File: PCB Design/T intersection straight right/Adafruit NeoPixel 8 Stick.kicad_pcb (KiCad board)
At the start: 2 copper layers, 36.6 x 28.6 mm, 8 parts, among them CN1 1X4SMT, CN2 1X4SMT, CN3 1X4SMT

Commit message: t straight fix
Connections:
- CN3 pad 3: Net-(CN3-Pad3) -> GND
- D4 pad 2: Net-(CN3-Pad3) -> unconnected-(D4-Pad2)
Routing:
- net Net-(CN3-Pad3): track 3.24 -> 0.00 mm, vias 1 -> 0
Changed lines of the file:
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@@
   (net 5 "+5V")
   (net 6 "Net-(CN2-Pad3)")
-  (net 7 "Net-(CN3-Pad3)")
+  (net 7 "unconnected-(D4-Pad2)")
   (net 8 "Net-(CN3-Pad4)")
   (net 9 "Net-(D1-Pad2)")
@@
       (net 5 "+5V") (pinfunction "VDD") (pintype "power_in"))
     (pad "2" smd rect (at -2.45 1.6 90) (size 1.5 1) (layers "F.Cu" "F.Paste" "F.Mask")
-      (net 7 "Net-(CN3-Pad3)") (pinfunction "DOUT") (pintype "output"))
+      (net 7 "unconnected-(D4-Pad2)") (pinfunction "DOUT") (pintype "output"))
     (pad "3" smd rect (at 2.45 1.6 90) (size 1.5 1) (layers "F.Cu" "F.Paste" "F.Mask")
       (net 1 "GND") (pinfunction "VSS") (pintype "power_in"))
@@
       (net 3 "Net-(CN1-Pad2)") (pinfunction "2") (pintype "bidirectional") (solder_mask_margin 0.1016))
     (pad "3" smd rect (at -0.92 0 180) (size 1.5 3.8) (layers "B.Cu" "B.Paste" "B.Mask")
-      (net 7 "Net-(CN3-Pad3)") (pinfunction "3") (pintype "bidirectional") (solder_mask_margin 0.1016))
+      (net 1 "GND") (pinfunction "3") (pintype "bidirectional") (solder_mask_margin 0.1016))
     (pad "4" smd rect (at 2.08 0 180) (size 1.5 3.8) (layers "B.Cu" "B.Paste" "B.Mask")
       (net 8 "Net-(CN3-Pad4)") (pinfunction "4") (pintype "bidirectional") (solder_mask_margin 0.1016))
@@
   (via (at 125.984 102.87) (size 0.8) (drill 0.4) (layers "F.Cu" "B.Cu") (net 5))
   (via (at 155.702 106.172) (size 0.8) (drill 0.4) (layers "F.Cu" "B.Cu") (net 6))
-  (segment (start 142.316 94.564) (end 142.316 97.7) (width 0.25) (layer "F.Cu") (net 7))
-  (segment (start 142.24 94.488) (end 142.316 94.564) (width 0.25) (layer "F.Cu") (net 7))
-  (via (at 142.24 94.488) (size 0.8) (drill 0.4) (layers "F.Cu" "B.Cu") (net 7))
   (via (at 139.192 92.964) (size 0.8) (drill 0.4) (layers "F.Cu" "B.Cu") (net 8))
   (segment (start 148.151782 104.233041) (end 148.151782 106.481782) (width 0.25) (layer "F.Cu") (net 9))

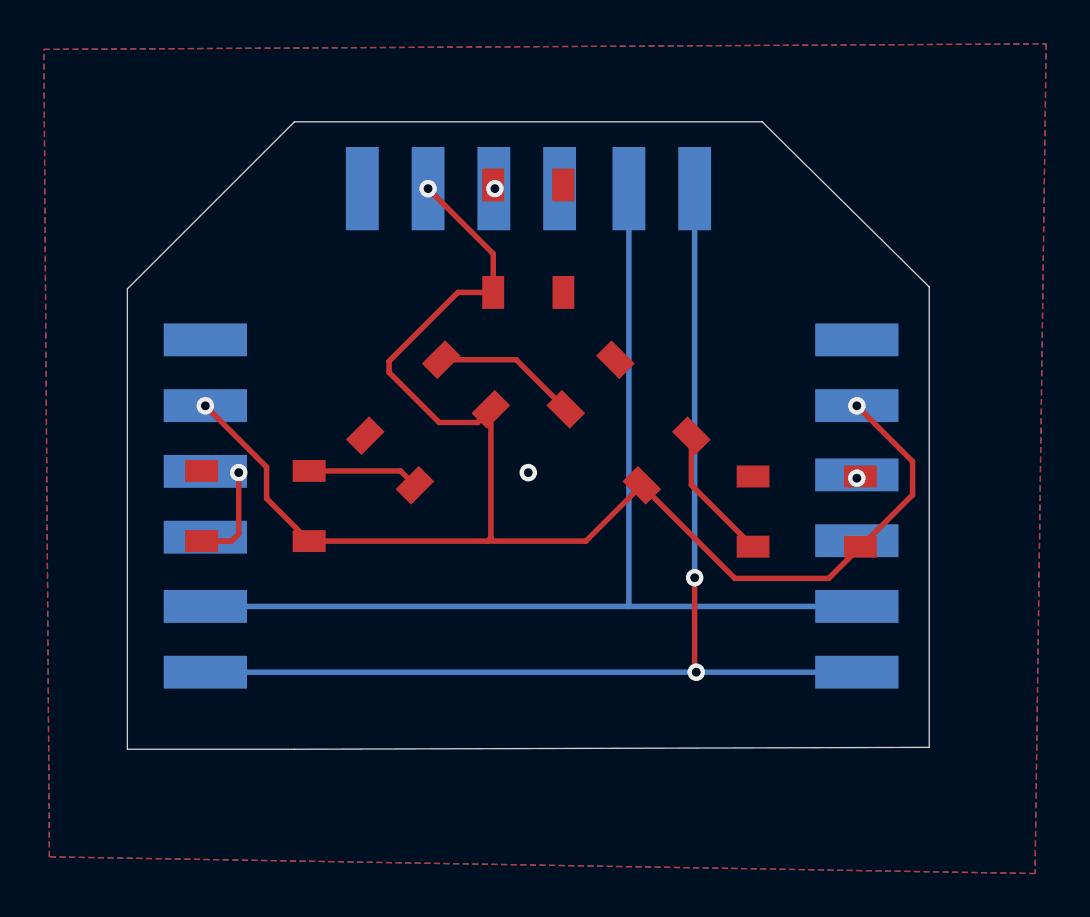
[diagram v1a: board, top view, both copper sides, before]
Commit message: move vias off pads
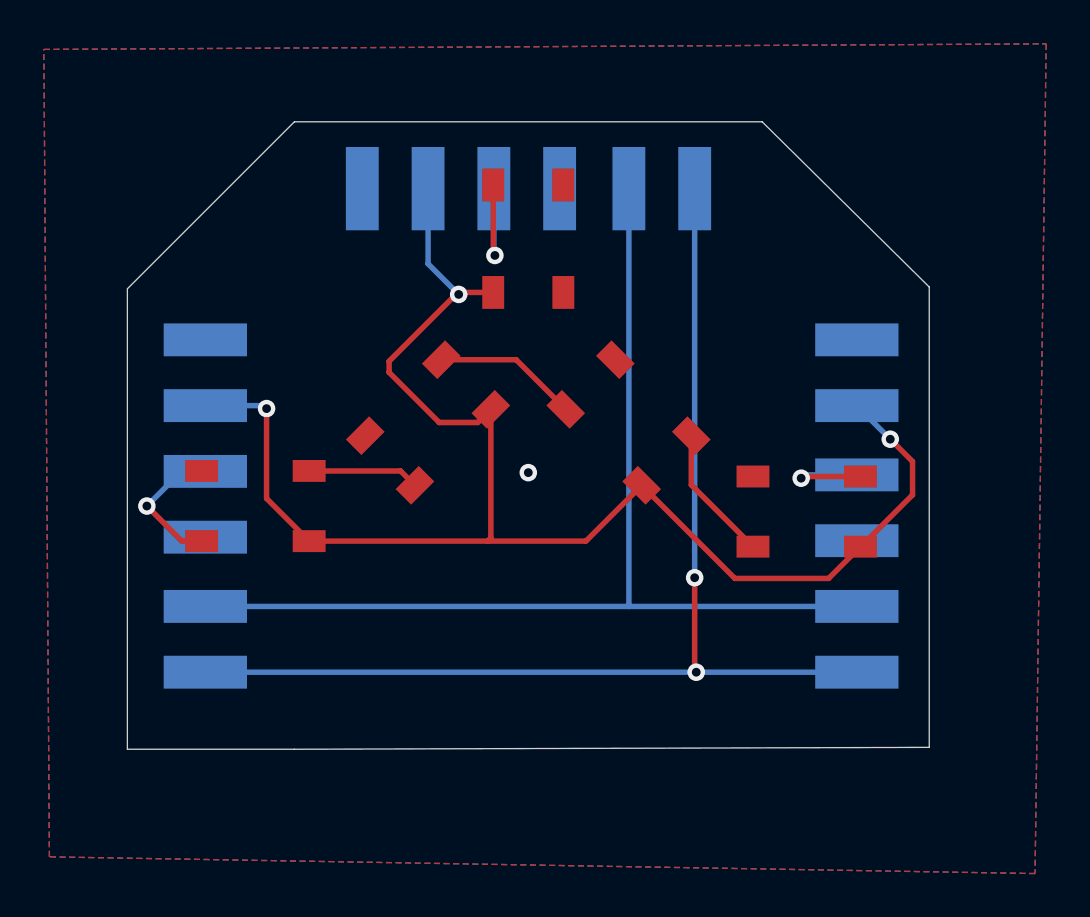
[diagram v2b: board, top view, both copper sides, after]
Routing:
- net Net-(CN3-Pad4): track 0.00 -> 6.31 mm
- net Net-(CN2-Pad3): track 0.00 -> 5.34 mm
- net Net-(CN1-Pad4): track 4.62 -> 6.49 mm
- net +5V: track 69.6 -> 70.6 mm
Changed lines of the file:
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@@
   (segment (start 125.984 112.022) (end 145.296 112.022) (width 0.25) (layer "B.Cu") (net 3))
   (segment (start 145.296 112.022) (end 155.702 112.022) (width 0.25) (layer "B.Cu") (net 3))
-  (segment (start 127.508 105.918) (end 127.508 108.712) (width 0.25) (layer "F.Cu") (net 4))
-  (segment (start 127.508 108.712) (end 127.178 109.042) (width 0.25) (layer "F.Cu") (net 4))
-  (segment (start 127.178 109.042) (end 125.82 109.042) (width 0.25) (layer "F.Cu") (net 4))
-  (via (at 127.508 105.918) (size 0.8) (drill 0.4) (layers "F.Cu" "B.Cu") (net 4))
+  (segment (start 125.82 109.042) (end 124.917 109.042) (width 0.25) (layer "F.Cu") (net 4))
+  (segment (start 124.917 109.042) (end 123.317 107.442) (width 0.25) (layer "F.Cu") (net 4))
+  (via (at 123.317 107.442) (size 0.8) (drill 0.4) (layers "F.Cu" "B.Cu") (net 4))
+  (segment (start 125.984 105.862) (end 124.897 105.862) (width 0.25) (layer "B.Cu") (net 4))
+  (segment (start 124.897 105.862) (end 123.317 107.442) (width 0.25) (layer "B.Cu") (net 4))
   (segment (start 130.72 109.042) (end 138.862 109.042) (width 0.25) (layer "F.Cu") (net 5))
-  (segment (start 139.116 95.936) (end 139.116 97.7) (width 0.25) (layer "F.Cu") (net 5))
-  (segment (start 128.778 107.1) (end 130.72 109.042) (width 0.25) (layer "F.Cu") (net 5))
+  (segment (start 128.778 107.1) (end 128.778 102.997) (width 0.25) (layer "F.Cu") (net 5))
+  (segment (start 130.72 109.042) (end 128.778 107.1) (width 0.25) (layer "F.Cu") (net 5))
+  (segment (start 158.242 105.41) (end 157.226 104.394) (width 0.25) (layer "F.Cu") (net 5))
   (segment (start 139.007782 103.030959) (end 139.007782 108.896218) (width 0.25) (layer "F.Cu") (net 5))
   (segment (start 139.007782 108.896218) (end 138.862 109.042) (width 0.25) (layer "F.Cu") (net 5))
@@
   (segment (start 134.366 101.346) (end 136.652 103.632) (width 0.25) (layer "F.Cu") (net 5))
   (segment (start 136.652 103.632) (end 138.406741 103.632) (width 0.25) (layer "F.Cu") (net 5))
-  (segment (start 125.984 102.87) (end 128.778 105.664) (width 0.25) (layer "F.Cu") (net 5))
   (segment (start 139.116 97.7) (end 137.504 97.7) (width 0.25) (layer "F.Cu") (net 5))
   (segment (start 158.242 106.934) (end 155.88 109.296) (width 0.25) (layer "F.Cu") (net 5))
   (segment (start 158.242 105.41) (end 158.242 106.934) (width 0.25) (layer "F.Cu") (net 5))
-  (segment (start 136.144 92.964) (end 139.116 95.936) (width 0.25) (layer "F.Cu") (net 5))
-  (segment (start 155.702 102.87) (end 158.242 105.41) (width 0.25) (layer "F.Cu") (net 5))
   (segment (start 138.862 109.042) (end 143.342823 109.042) (width 0.25) (layer "F.Cu") (net 5))
   (segment (start 154.418 110.744) (end 155.866 109.296) (width 0.25) (layer "F.Cu") (net 5))
-  (segment (start 128.778 105.664) (end 128.778 107.1) (width 0.25) (layer "F.Cu") (net 5))
   (segment (start 143.342823 109.042) (end 145.889041 106.495782) (width 0.25) (layer "F.Cu") (net 5))
   (segment (start 138.406741 103.632) (end 139.007782 103.030959) (width 0.25) (layer "F.Cu") (net 5))
@@
   (segment (start 137.504 97.7) (end 134.366 100.838) (width 0.25) (layer "F.Cu") (net 5))
   (segment (start 145.889041 106.495782) (end 150.137259 110.744) (width 0.25) (layer "F.Cu") (net 5))
-  (via (at 155.702 102.87) (size 0.8) (drill 0.4) (layers "F.Cu" "B.Cu") (net 5))
-  (via (at 136.144 92.964) (size 0.8) (drill 0.4) (layers "F.Cu" "B.Cu") (net 5))
-  (via (at 125.984 102.87) (size 0.8) (drill 0.4) (layers "F.Cu" "B.Cu") (net 5))
-  (via (at 155.702 106.172) (size 0.8) (drill 0.4) (layers "F.Cu" "B.Cu") (net 6))
-  (via (at 139.192 92.964) (size 0.8) (drill 0.4) (layers "F.Cu" "B.Cu") (net 8))
+  (via (at 157.226 104.394) (size 0.8) (drill 0.4) (layers "F.Cu" "B.Cu") (net 5))
+  (via (at 137.541 97.79) (size 0.8) (drill 0.4) (layers "F.Cu" "B.Cu") (net 5))
+  (via (at 128.778 102.997) (size 0.8) (drill 0.4) (layers "F.Cu" "B.Cu") (net 5))
+  (segment (start 155.702 102.87) (end 157.226 104.394) (width 0.25) (layer "B.Cu") (net 5))
+  (segment (start 125.984 102.862) (end 128.643 102.862) (width 0.25) (layer "B.Cu") (net 5))
+  (segment (start 136.144 96.393) (end 137.541 97.79) (width 0.25) (layer "B.Cu") (net 5))
+  (segment (start 155.702 102.862) (end 155.702 102.87) (width 0.25) (layer "B.Cu") (net 5))
+  (segment (start 128.643 102.862) (end 128.778 102.997) (width 0.25) (layer "B.Cu") (net 5))
+  (segment (start 136.144 92.964) (end 136.144 96.393) (width 0.25) (layer "B.Cu") (net 5))
+  (segment (start 153.162 106.172) (end 153.238 106.096) (width 0.25) (layer "F.Cu") (net 6))
+  (segment (start 153.238 106.096) (end 155.866 106.096) (width 0.25) (layer "F.Cu") (net 6))
+  (via (at 153.162 106.172) (size 0.8) (drill 0.4) (layers "F.Cu" "B.Cu") (net 6))
+  (segment (start 153.162 106.172) (end 153.312 106.022) (width 0.25) (layer "B.Cu") (net 6))
+  (segment (start 153.312 106.022) (end 155.702 106.022) (width 0.25) (layer "B.Cu") (net 6))
+  (segment (start 139.116 95.936) (end 139.116 92.8) (width 0.25) (layer "F.Cu") (net 8))
+  (segment (start 139.192 96.012) (end 139.116 95.936) (width 0.25) (layer "F.Cu") (net 8))
+  (via (at 139.192 96.012) (size 0.8) (drill 0.4) (layers "F.Cu" "B.Cu") (net 8))
+  (segment (start 139.144 92.964) (end 139.144 95.964) (width 0.25) (layer "B.Cu") (net 8))
+  (segment (start 139.144 95.964) (end 139.192 96.012) (width 0.25) (layer "B.Cu") (net 8))
   (segment (start 148.151782 104.233041) (end 148.151782 106.481782) (width 0.25) (layer "F.Cu") (net 9))
   (segment (start 148.151782 106.481782) (end 150.966 109.296) (width 0.25) (layer "F.Cu") (net 9))
